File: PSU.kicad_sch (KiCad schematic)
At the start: 0 parts

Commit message: Started the power circuit schematic sheet
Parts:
- added D10, D11: ESD9B5.0ST5G, A_HDJ_Library:D_0402_1005Metric, symbol Diode:ESD9B5.0ST5G
- added D12, D13, D14: D_Zener, A_HDJ_Library:D_0402_1005Metric, symbol Device:D_Zener
- added J17: Barrel_Jack_Switch, symbol Connector:Barrel_Jack_Switch
- added J18: USB_C_Receptacle_USB2.0_16P, symbol Connector:USB_C_Receptacle_USB2.0_16P
- added U78: USB PD等快充协议受电芯片-CH224K-ESSOP10, ESSOP10, symbol A_HDJ_Library:CH224K
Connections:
- new net: D11.2 (A2), U78.4 (DP)
- new net: D10.2 (A2), J18.A7 (D-), J18.B7 (D-), U78.5 (DM)
- new net: D14.1 (K), J18.B5 (CC2), U78.6 (CC2)
- new net: D13.1 (K), J18.A5 (CC1), U78.7 (CC1)
- new net: D12.1 (K), J18.A4 (VBUS), J18.A9 (VBUS), J18.B4 (VBUS), J18.B9 (VBUS)
- new net: J18.A6 (D+), J18.B6 (D+)
- new net GND: D10.1 (A1), D11.1 (A1), D12.2 (A), D13.2 (A), D14.2 (A), J18.A1 (GND), J18.A12 (GND), J18.B1 (GND), J18.B12 (GND), J18.SH (SHIELD)
- no-connect marks 0 -> 2

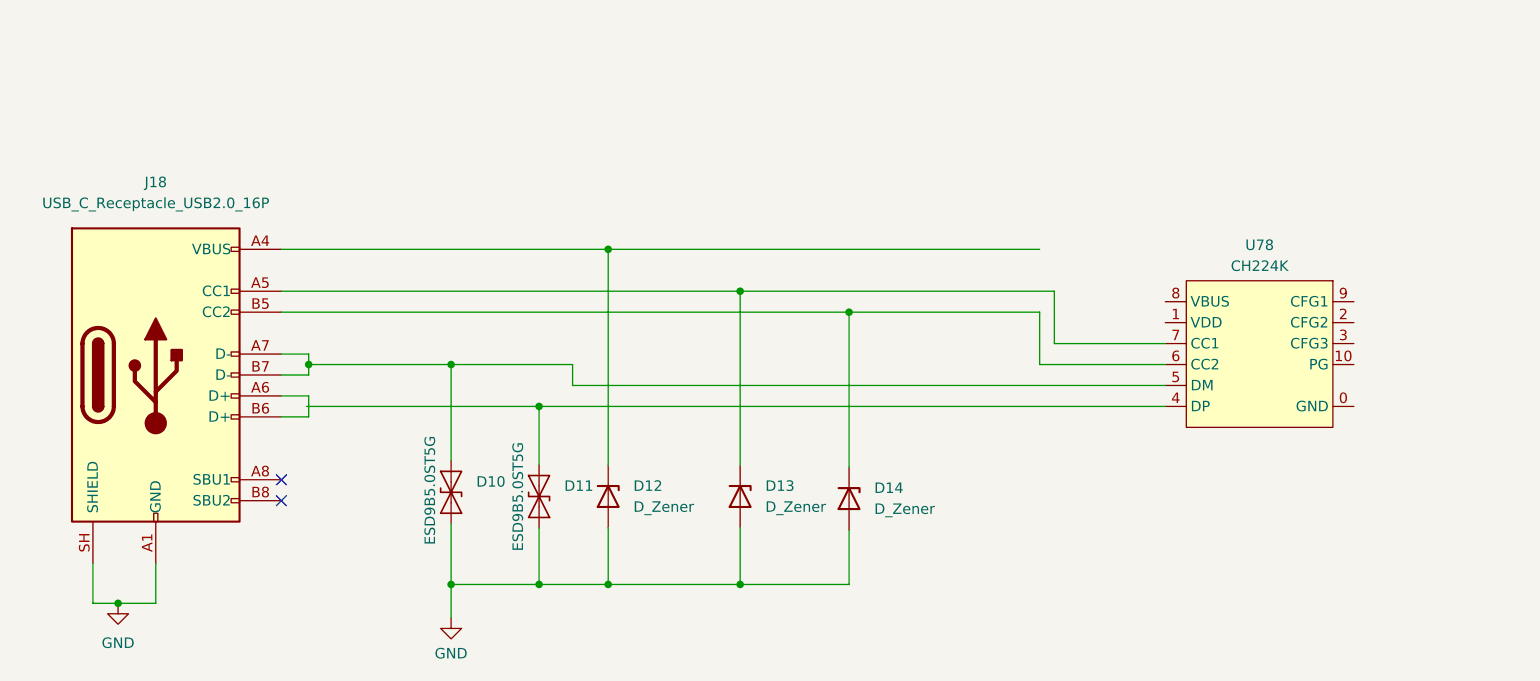
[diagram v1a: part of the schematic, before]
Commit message: wired up the power management ic to the usbc j connector
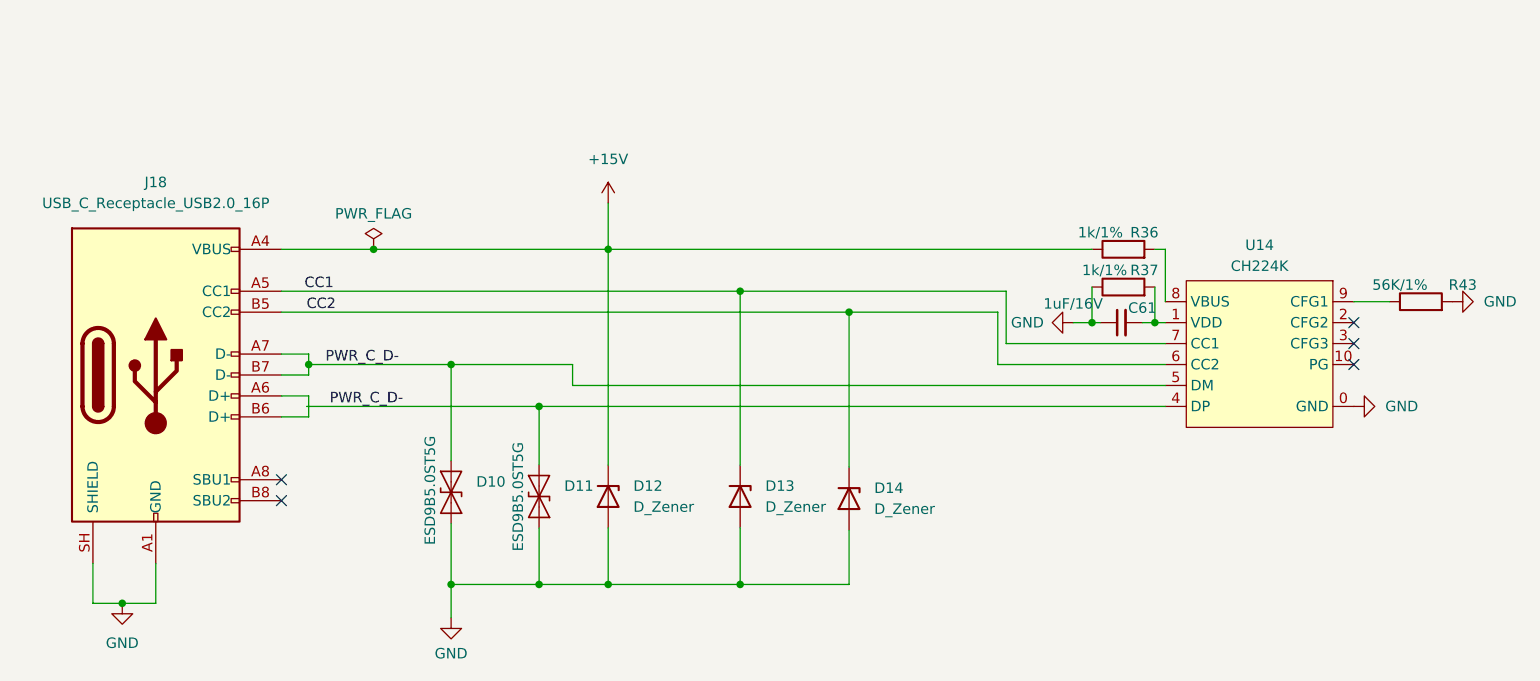
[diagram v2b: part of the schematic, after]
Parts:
- added C61: 1uF/16V, A_HDJ_Library:C_0402_1005Metric, symbol Device:C_Small
- added R36, R37: 1k/1%, A_HDJ_Library:R_0402_1005Metric, symbol Device:R
- added R43: 56K/1%, symbol Device:R
- renumbered U78 to U14
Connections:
- net GND: now also U14.0 (GND), C61.1, R37.1, R43.2
- net PWR_C_D-: now reaches D11.2 (A2), U14.4 (DP)
- net PWR_C_D-: now also D10.2 (A2), J18.A7 (D-), J18.B7 (D-), U14.5 (DM)
- net at U14.1 (VDD): now also C61.2, R37.2
- net CC2: now reaches D14.1 (K), J18.B5 (CC2), U14.6 (CC2)
- net CC1: now reaches D13.1 (K), J18.A5 (CC1), U14.7 (CC1)
- net at U14.8 (VBUS): now also R36.2
- net at U14.9 (CFG1): now also R43.1
- net +15V: now reaches D12.1 (K), J18.A4 (VBUS), J18.A9 (VBUS), J18.B4 (VBUS), J18.B9 (VBUS)
- net +15V: now also R36.1
- no-connect marks 2 -> 5

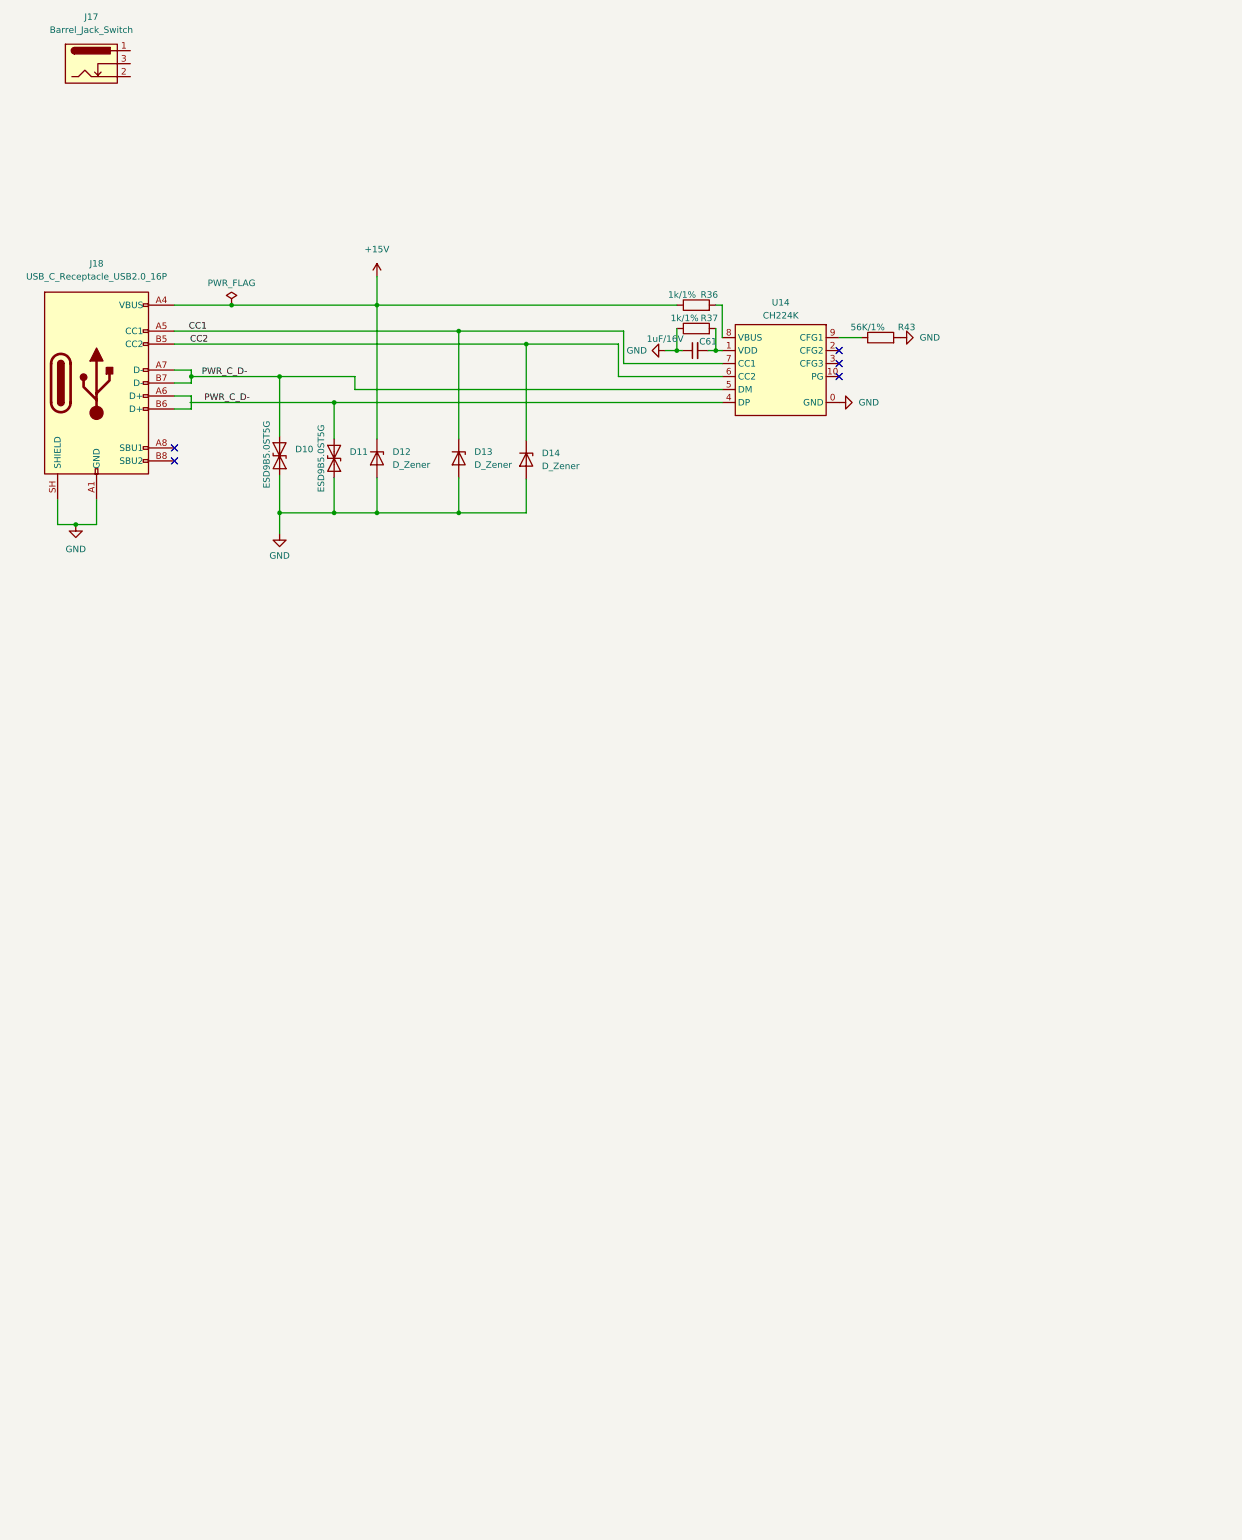
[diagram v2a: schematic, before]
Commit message: Added the circuit for the barrel jack in the PSU schematic sheet
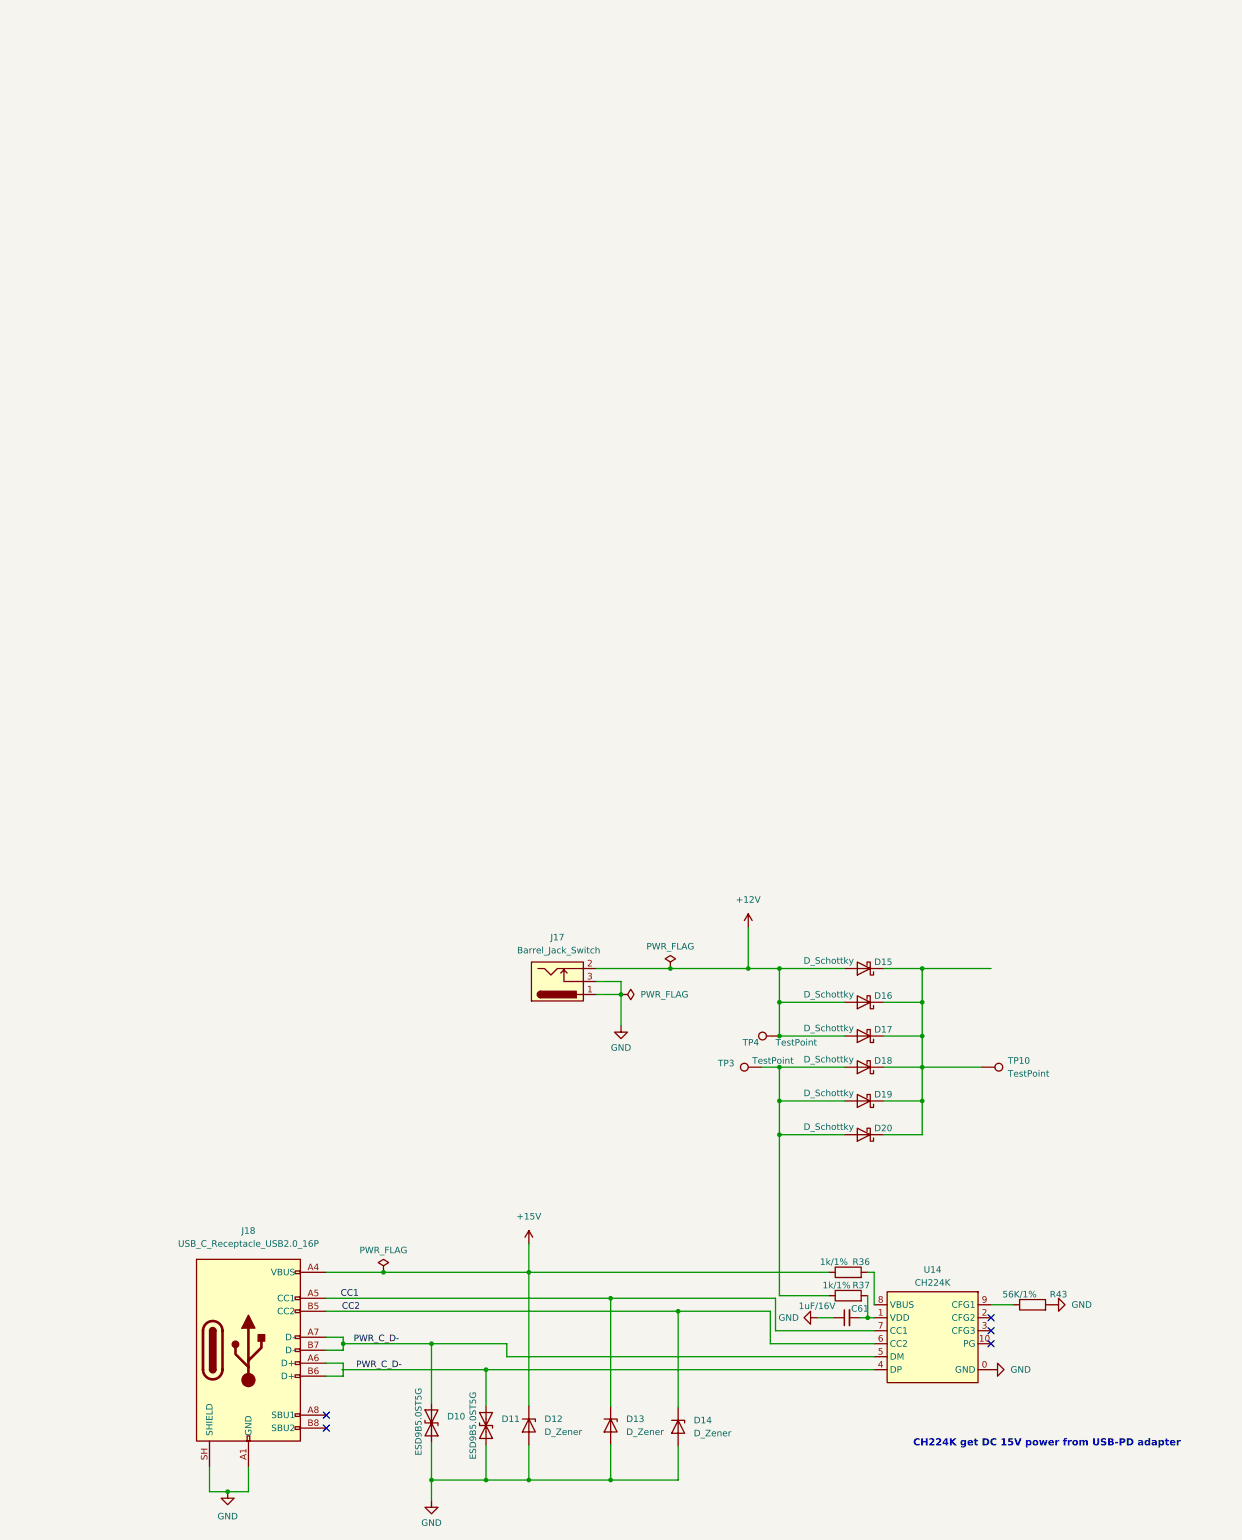
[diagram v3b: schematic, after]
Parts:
- added D15, D16, D17, D18, D19, D20: D_Schottky, A_HDJ_Library:D_SMA, symbol Device:D_Schottky
- added TP10, TP3, TP4: TestPoint, symbol Connector:TestPoint
- J17: footprint (none) -> A_HDJ_Library:DC_Jack_DC007B_30V_10A
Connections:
- net GND: now also J17.1, J17.3; no longer R37.1
- net +12V: now reaches J17.2
- net +12V: now also D15.2 (A), D16.2 (A), D17.2 (A), TP4.1
- new net: D15.1 (K), D16.1 (K), D17.1 (K), D18.1 (K), D19.1 (K), D20.1 (K), TP10.1
- new net: D18.2 (A), D19.2 (A), D20.2 (A), R37.1, TP3.1
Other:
- note added: "CH224K get DC 15V power from USB-PD adapter"
- moved on the sheet: C61, D10, D11, D12, D13, D14, J17, J18, R36, R37, R43, U14

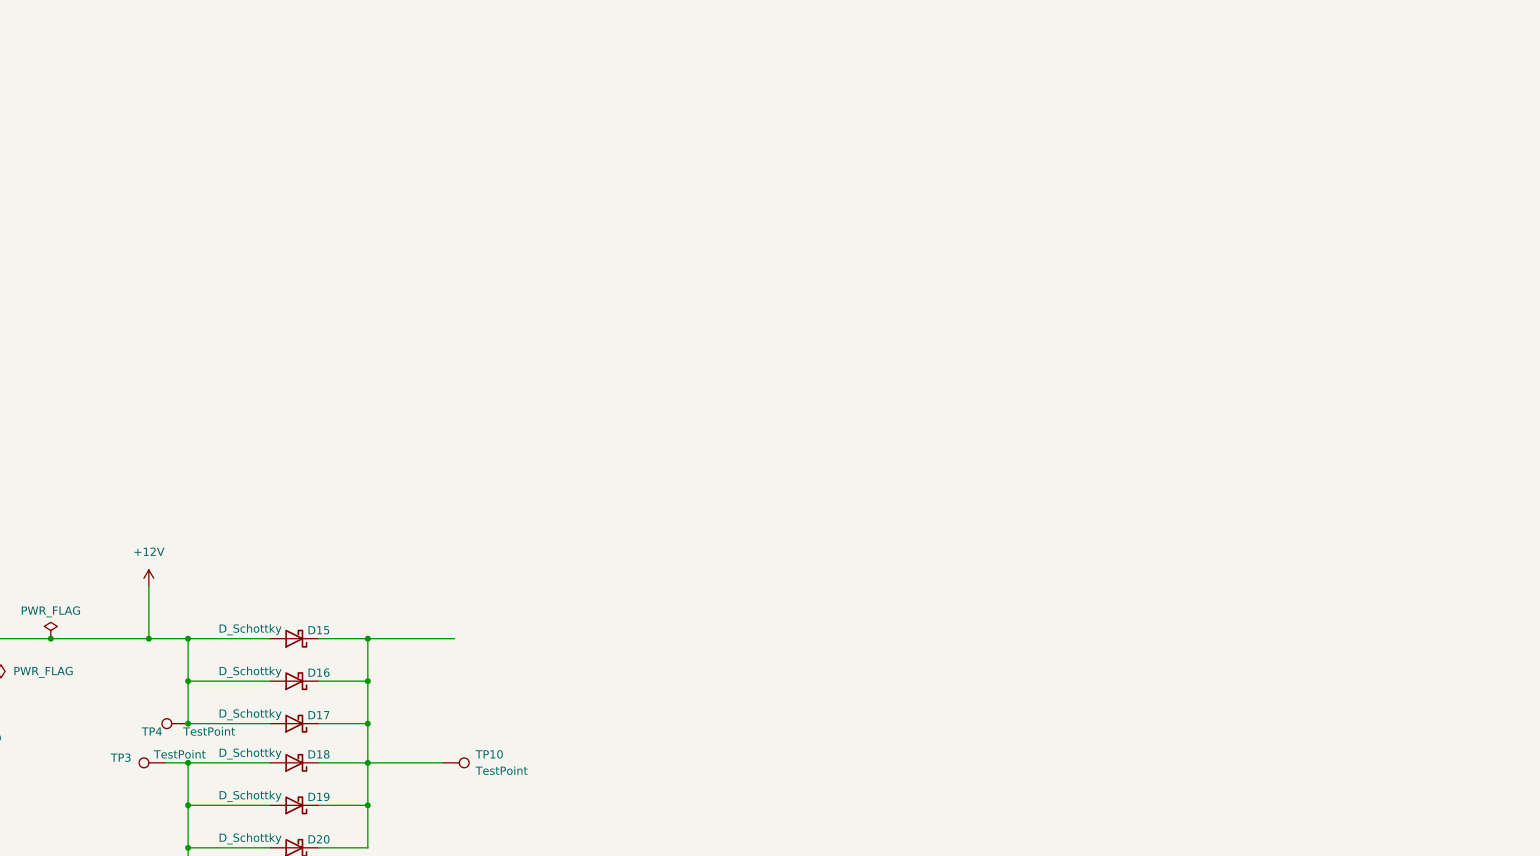
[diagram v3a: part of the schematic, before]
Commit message: Populated the PCU with passive parts inline before wiring up the schematic and finding correct IC's to intefrate into the system
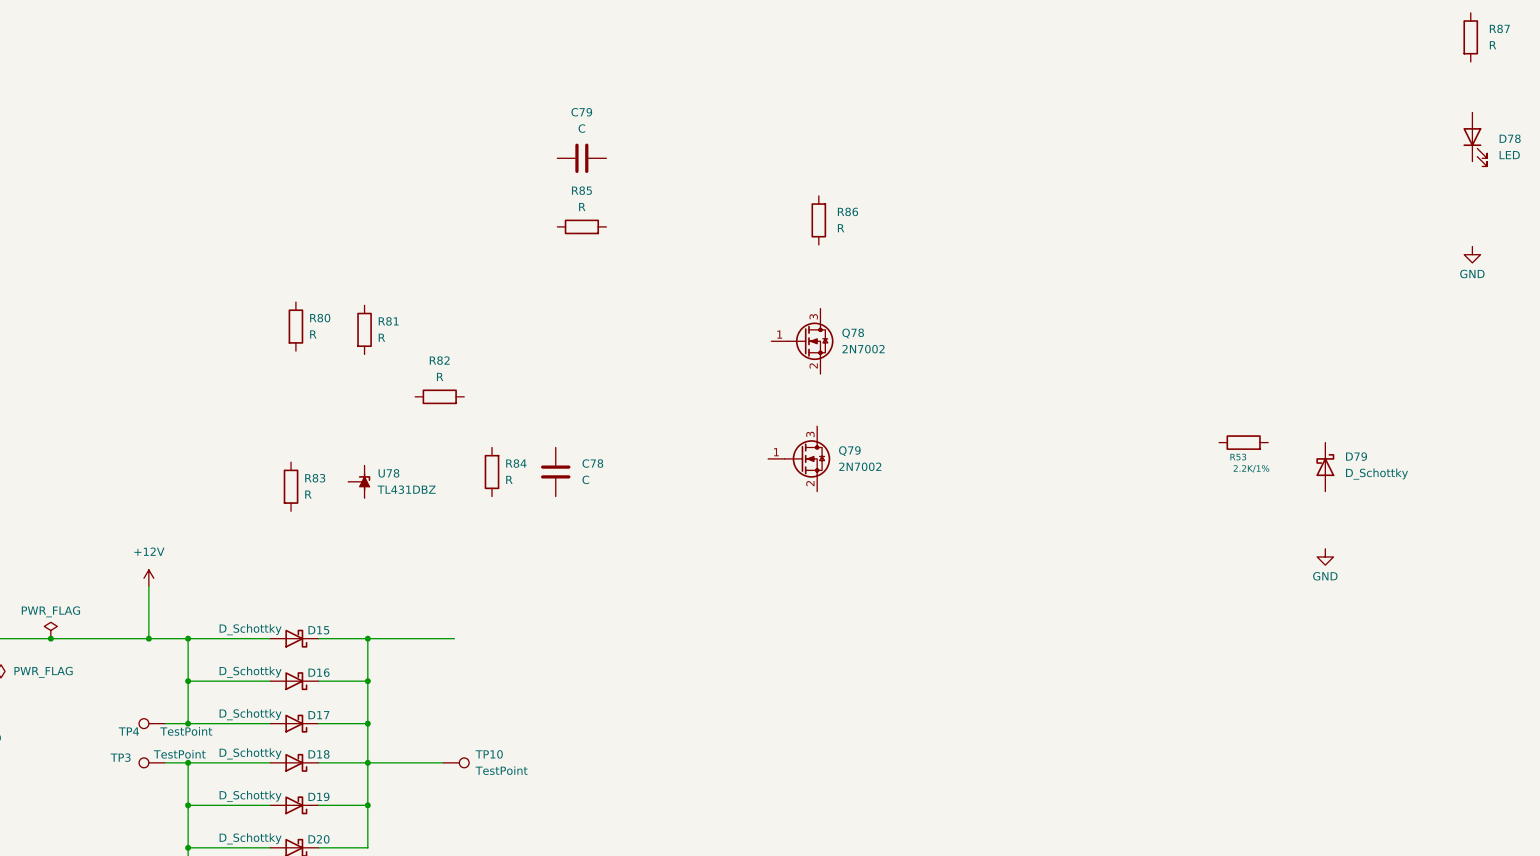
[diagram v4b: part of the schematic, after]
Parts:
- added C78, C79: C, symbol Device:C
- added D78: LED, symbol Device:LED
- added D79: D_Schottky, symbol Device:D_Schottky
- added Q78, Q79: 2N7002, Package_TO_SOT_SMD:SOT-23, symbol Transistor_FET:2N7002
- added R53: 2.2K/1%, A_HDJ_Library:R_0402_1005Metric, symbol Device:R
- added R80, R81, R82, R83, R84, R85, R86, R87: R, symbol Device:R
- added U78: TL431DBZ, Package_TO_SOT_SMD:SOT-23, symbol Reference_Voltage:TL431DBZ
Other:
- moved on the sheet: TP4
